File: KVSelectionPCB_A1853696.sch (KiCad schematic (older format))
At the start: 0 parts

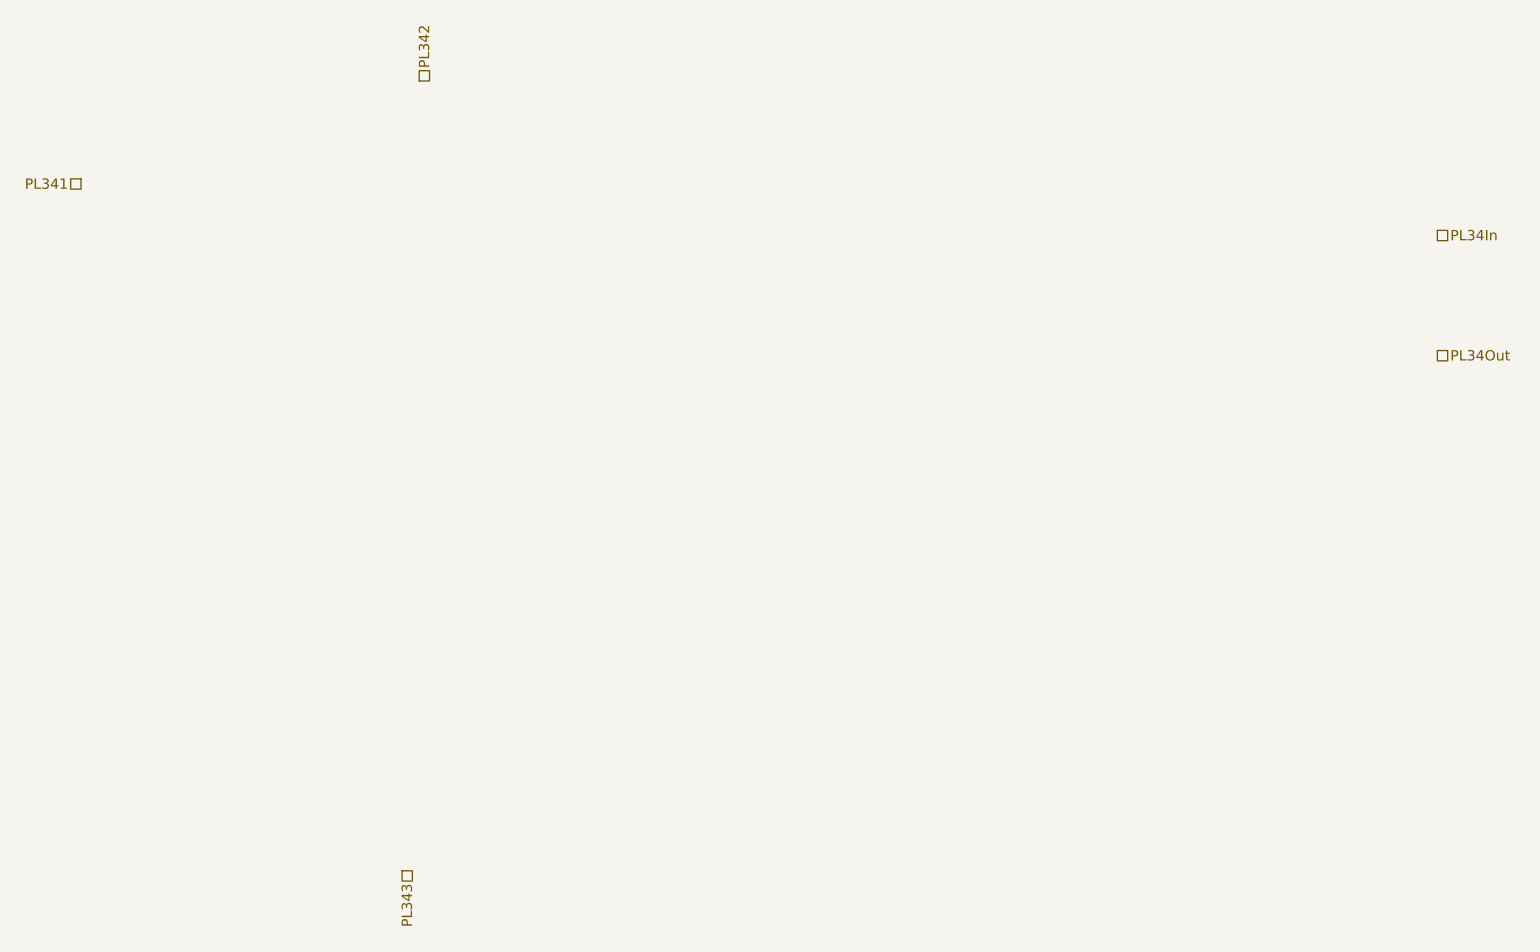
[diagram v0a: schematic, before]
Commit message: added ColumnWiring, DataSystemAutoReset, KVSelection and VacuumInterlock
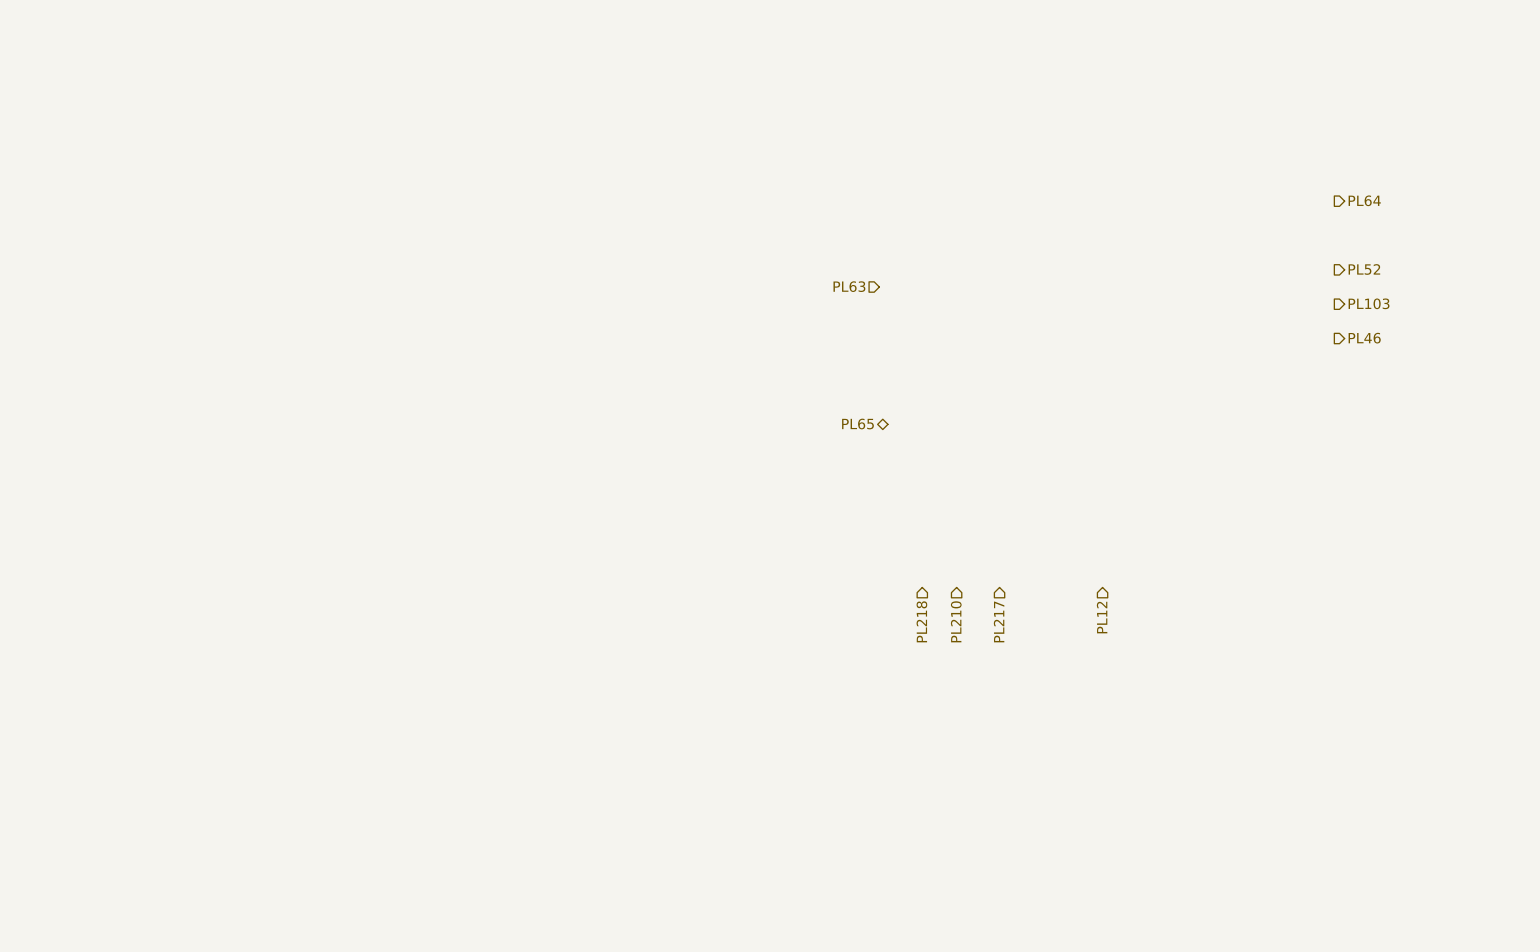
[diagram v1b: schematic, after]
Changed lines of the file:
@@
 $Descr A4 11693 8268
 encoding utf-8
-Sheet 9 25
+Sheet 23 25
 Title ""
 Date ""
@@
 Comment4 ""
 $EndDescr
-Text HLabel 1800 1900 0    60   UnSpc ~ 0
-PL341
-Text HLabel 3800 1300 1    60   UnSpc ~ 0
-PL342
-Text HLabel 3700 5900 3    60   UnSpc ~ 0
-PL343
-Text HLabel 9700 2200 2    60   UnSpc ~ 0
-PL34In
-Text HLabel 9700 2900 2    60   UnSpc ~ 0
-PL34Out
+Text HLabel 9100 2000 2    60   Output ~ 0
+PL64
+Text HLabel 9100 2400 2    60   Output ~ 0
+PL52
+Text HLabel 9100 2600 2    60   Output ~ 0
+PL103
+Text HLabel 9100 2800 2    60   Output ~ 0
+PL46
+Text HLabel 7750 4250 3    60   Input ~ 0
+PL12
+Text HLabel 7150 4250 3    60   Input ~ 0
+PL217
+Text HLabel 6900 4250 3    60   Input ~ 0
+PL210
+Text HLabel 6700 4250 3    60   Input ~ 0
+PL218
+Text HLabel 6500 3300 0    60   BiDi ~ 0
+PL65
+Text HLabel 6450 2500 0    60   Input ~ 0
+PL63
 $EndSCHEMATC
